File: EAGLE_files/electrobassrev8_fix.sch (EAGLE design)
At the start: 234 parts, among them IC1 CY8C58LPXXX, IC18 CY8C4124, IC2 4052D, IC3 LMV321M5, IC5 LMV321M5, IC6 LM324D, J1 105162-0001, J28 PJ-066A, Q1 DMP3099L, U1 ES_DAISY_SEED_DOUBLE, U2 LP2985, U7 ES_DAISY_SEED_DOUBLE, X1 3P-2MM-TH-MALE, X10 3P-2MM-TH-MALE, X11 3P-2MM-TH-MALE, X12 3P-2MM-TH-MALE, X13 3P-2MM-TH-MALE, X14 3P-2MM-TH-MALE, X15 3P-2MM-TH-MALE, X16 332-02, X17 332-02, X18 332-02, X19 332-02, X2 NRJ6HF2, X3 NRJ6HF2, X4 USB+SHIELD, X5 332-02, X6 332-02, X7 332-02, X8 332-02, X9 3P-2MM-TH-MALE

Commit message: changes to how presets are loaded
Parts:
- removed 0_6: (no value), adafruit:PINHD-1X1
- removed IC1: CY8C58LPXXX, cypress:CY8C58LPXXX
- removed JP17, JP18, JP19: PINHD-2X5, Connector:PINHD-2X5
- removed JP20, JP21: 20021121, custom:20021121
- removed R47, R51, R52, R53, R54: 0R_DNP, adafruit:R-US_R0603
- removed U$7: CY8CKIT-059_TARGET_3, CY8KIT-059:CY8CKIT-059_TARGET_3
- added 12VD1: (no value), adafruit:PINHD-1X1
- added C15, C19, C22, C23, C24, C25: 10uf, rcl:C-EUC1206K
- added C16, C31, C32, C33, C36, C45, C46: 1uf, rcl:C-EUC0603
- added C17: .001uf, rcl:C-EUC0603
- added C18: .01uf, adafruit:C-USC0603K
- added C20, C21: 22uf, rcl:C-EUC1206K
- added C26, C28, C30, C40, C41, C42, C43, C44: .1uf, rcl:C-USC0603K
- added C29: 2200pf, adafruit:C-USC0603K
- added J2, J3, J5, J6, J7, J8: SM06B-SRSS-TB(LF)(SN), sm06b:SM06B-SRSS-TB(LF)(SN)
- added JP5: 20021121, custom:20021121
- added L1: 2.2uH, Electrosmith-Passives:INDUCTORS
- added R27, R36: 20k, Resistor:R-US_R0603
- added R34, R35: 10k, Resistor:R-US_R0603
- added R37: 22R, rcl:R-US_R0603
- added R56, R57, R88, R89, R90: 2M, Electrosmith-Passives:R-US_R0603
- added R91, R92: 100R, Electrosmith-Passives:R-US_R0603
- added R93, R94, R95, R96, R97: 47k, rcl:R-US_R0603
- added U$9: POWER_ISOLATE, Electrosmith-IC:POWER_ISOLATE
- added U10: OPA1654, Electrosmith-IC:OPA1654_TSSOP-14
- added U3: MCP1755T-5002E/DCSOT-223_5_MCH-M, MCP1755T:MCP1755T-5002E/DCSOT-223_5_MCH-M
- added U4: CY8C5888LTI-LP097QFN-68-M, cy8c:CY8C5888LTI-LP097QFN-68-M
- added U5: ADUM3160BRWZRW_16_ADI-M, MCP1755T:ADUM3160BRWZRW_16_ADI-M
- R23: value 0R -> 2M; device adafruit:R-US_R0603 -> Electrosmith-Passives:R-US_R0603; PARTNO CRCW06030000Z0EAHP -> (none)
- R32: value 1.6k -> 5R_DNP; PARTNO ESR03EZPJ152 -> CRCW06030000Z0EAHP
- R41: value 1.6k -> 22R; device adafruit:R-US_R0603 -> rcl:R-US_R0603; PARTNO ESR03EZPJ152 -> RC0603JR-0747RL
- R45, R46: value 0R_DNP -> 22R; device adafruit:R-US_R0603 -> rcl:R-US_R0603; PARTNO *DNP -> RC0603JR-0747RL
- R50: value 0R -> 5R
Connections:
- net N$66 renamed ADC4OPAMPOUT
- removed net ADC1_2: R53.1, U7.GPIO15(ADC0)
- removed net ADC2_2: R51.1, U7.GPIO16(ADC1)
- removed net ADC3_2: R54.1, U7.GPIO17(ADC2)
- removed net ADC4_2: R52.1, U7.GPIO18(ADC3)
- removed net ADC5_1: U1.GPIO19(ADC4)
- removed net ADC5_2: U7.GPIO19(ADC4)
- removed net ADC6_1: U1.GPIO20(ADC5)
- removed net ADC6_2: U7.GPIO20(ADC5)
- removed net ADC7_1: U1.GPIO21(ADC6)
- removed net ADC7_2: U7.GPIO21(ADC6)
- removed net ADC8_1: U1.GPIO22(ADC7/DAC2)
- removed net ADC8_2: U7.GPIO22(ADC7/DAC2)
- removed net DAISY_D+: R45.1, U7.GPIO30(USB_HS_D+)
- removed net DAISY_D-: R47.1, U7.GPIO29(USB_HS_D_-)
- removed net EXTRA_GPIO: 0_6.1, U$7.P_0.6
- removed net PA0_VBUS: R23.1, U7.GPIO25(ADC10)
- removed net PICKUP2_OUT: JP19.2, JP21.P$10, JP21.P$9
- removed net PICKUP3_OUT: JP19.3, JP21.P$7, JP21.P$8
- removed net SCL_GN: R41.2, U1.GPIO11(I2C1_SCL), U7.GPIO11(I2C1_SCL)
- removed net SDA_GN: R32.2, U1.GPIO12(I2C1_SDA), U7.GPIO12(I2C1_SDA)
- new net +5V_ISOL: C20.1, C28.1, R23.2, R88.2, U$9.OUT+, U10P.V+
- new net 5V0: C15.1, C16.1, C17.1, C18.1, C21.1, L1.P$1, U3.VOUT
- new net ADC1OPAMPOUT: C4.2, IC6A.OUT, R1.1, R81.2
- new net ADC2OPAMPOUT: C9.2, IC6B.OUT, R24.1, R80.2
- new net ADC3OPAMPOUT: C10.2, IC6C.OUT, R26.1, R83.2
- new net ADCBYPASS: C31.1, U4.P0[3]_(GPIO
- new net AGND4: G1.1, JP15.4, JP15.6, X2.S
- new net CMOD_CH0: C29.1, U4.P15[4]_(GPIO)
- new net GNDINT: C20.2, C28.2, JP1.4, JP4.10, R32.1, R34.2, R35.2, R56.1, R57.1, R89.1, R90.1, U$9.OUT-, U10P.V-
- new net GNDINT_KNOBS: JP3.10, U$2.P$2, U$2.P$6
- new net GNDIO: C30.2, JP1.8, JP22.4, U5.GND1, U5.GND1_2
- new net LOUT_2_INTOCN: C24.2, JP4.4, R57.2
- new net N$20: R35.1, R36.2, U10B.-IN
- new net N$21: S1.1, S1.4
- new net N$23: R37.1, U5.UD-
- new net N$24: R41.1, U5.UD+
- new net N$63: R45.2, U5.DD-
- new net N$64: R46.2, U5.DD+
- new net N$76: R27.1, R91.2, U10A.OUT
- new net N$77: C23.2, R88.1, R89.2, U10B.+IN
- new net N$78: R36.1, R92.2, U10B.OUT
- new net N$79: C24.1, R91.1
- new net N$80: C25.1, R92.1
- new net N$81: C19.1, L1.P$2, U$9.IN+
- new net PROG_RESET: JP5.P$10, U4.XRES
- new net PROG_SWDCLK: JP5.P$4, U4.(TCK
- new net PROG_SWDIO: JP5.P$2, U4.(TMS
- new net PROG_SWO: JP5.P$6, U4.(TDO
- new net ROUT_2_INTOCN: C25.2, JP4.2, R90.2
- new net SPI_READY: U1.GPIO6(SDMMC1_CK), U4.P0[6]_(GPIO, U7.GPIO0(USB_HS_ID)
- new net USBDM: R45.1, U4.(USBIO
- new net USBDP: R46.1, U4.(USBIO_2
- new net VCCA_1: C32.1, C42.1, U4.VCCA
- new net VCCD_1: C36.1, C40.1, U4.VCCD, U4.VCCD_2
- net +10V: now also J2.3, J2.4, J3.3, J3.4; no longer JP18.7, JP18.9
- net +3V3: now also C26.1, C43.1, C44.1, C45.1, C46.1, R93.2, R94.2, R95.2, R96.2, R97.2, U4.VDDD, U4.VDDD_2, U4.VDDIO0, U4.VDDIO1, U4.VDDIO2, U4.VDDIO3, U5.PIN, U5.SPD, U5.VBUS2, U5.VDD2; no longer R32.1, R41.1, U$7.VDD, U$7.VDDIO
- net 12VD1: now also 12VD1.1, U3.!SHDN, U3.VIN
- net 3V3A1: now also C33.1, C41.1, U4.VDDA; no longer R46.1
- net 3V3FORPEDAL: now also JP1.9; no longer JP1.7
- net ADC1_1: no longer C4.2, IC6A.OUT, R1.1, R53.2, R81.2
- net ADC2_1: no longer C9.2, IC6B.OUT, R24.1, R51.2, R80.2
- net ADC3_1: no longer C10.2, IC6C.OUT, R26.1, R54.2, R83.2
- net ADC4_1: no longer R52.2
- net AGND: now also C15.2, C16.2, C17.2, C18.2, C19.2, C21.2, C31.2, C32.2, C33.2, C41.2, C42.2, J2.2, J2.5, J3.2, J3.5, JP1.7, R32.2, U$9.IN-, U3.GND, U4.VSSA; no longer JP1.4, JP1.8, JP18.10, JP18.8, JP4.10, S1.1, S1.4
- net AGND3: now also JP15.7; no longer G1.1, JP15.4, JP15.6, X2.S
- net BLUE_LED: now also U4.P2[1]_(GPIO); no longer U$7.P_2.1
- net CAP_0_0: now also U4.P2[0]_(GPIO); no longer U$7.P_2.0
- net CAP_0_1: now also U4.P2[2]_(GPIO); no longer U$7.P_2.2
- net CAP_0_2: now also U4.P2[4]_(GPIO; no longer U$7.P_2.4
- net CAP_0_3: now also U4.(TRACEDATA[2]; no longer U$7.P_2.6
- net CAP_1_0: now also U4.(IDAC1; no longer U$7.P_3.0
- net CAP_1_1: now also U4.(OPAMP3+; no longer U$7.P_3.3
- net CAP_1_2: now also U4.(OPAMP1+; no longer U$7.P_3.5
- net CAP_1_3: now also U4.P3[7]_(GPIO; no longer U$7.P_3.7
- net CMOD_CH1: now also U4.(TDI; no longer U$7.P_1.4
- net CV_PEDAL: now also U4.(OPAMP1-; no longer U$7.P_3.4
- net CV_PEDAL_SENSE: now also U4.(OPAMP3-; no longer U$7.P_3.2
- net DGND: now also C26.2, C29.2, C36.2, C40.2, C43.2, C44.2, C45.2, C46.2, JP5.P$3, JP5.P$5, JP5.P$7, JP5.P$9, U4.EPAD, U4.VBAT, U4.VBOOST, U4.VSSB, U4.VSSD, U4.VSSD_2, U4.VSSD_3, U4.VSSD_4, U5.GND2, U5.GND2_2; no longer JP1.9, JP22.4, U$7.GND1, U$7.GND2, U$7.GND3
- net DGND3: no longer JP15.9
- net DM: now also R37.2; no longer R47.2
- net DOWN: now also U4.P15[3]_(GPIO; no longer U$7.P_15.3
- net DP: now also R41.2; no longer R45.2
- net EDIT: now also U4.P15[2]_(GPIO; no longer U$7.P_15.2
- net EXT_MUX_EN: now also U4.P15[5]_(GPOI); no longer U$7.P_15.5
- net EXT_MUX_S0: now also U4.(MHZ_XTAL:_XO; no longer U$7.P_15.0
- net EXT_MUX_S1: now also U4.(MHZ_XTAL:_XI; no longer U$7.P_15.1
- net FRETTED_LATCHING: now also U4.P12[3]_(SIO); no longer U$7.P_12.3
- net FRETTED_MOMENTARY: now also U4.P12[2]_(SIO); no longer U$7.P_12.2
- net IDAC_OUT: now also U4.P0[7]_(GPIO; no longer U$7.P_0.7
- net JOY_X: now also U4.P2[5]_(GPIO; no longer U$7.P_2.5
- net JOY_Y: now also U4.P2[3]_(GPIO; no longer U$7.P_2.3
- net KNOB_1: now also U4.P0[1]_(GPIO; no longer U$7.P_0.1
- net KNOB_2: now also U4.P3[6]_(GPIO; no longer U$7.P_3.6
- net LED_1: now also U4.P0[2]_(GPIO; no longer U$7.P_0.2
- net LOUT_2: now also C22.1; no longer JP4.4
- net MISO_1: now also U4.(GPIO)_P1[7]; no longer U$7.P_1.7
- net MISO_2: now also U4.(TRACEDATA[3]; no longer U$7.P_2.7
- net MOSI_1_P: now also U4.(SIO)_P12[6]; no longer U$7.P_12.6
- net MOSI_2_P: now also U4.(I2C0:_SCL; no longer U$7.P_12.4
- net N$45: no longer R46.2
- net N$56: now also JP15.9; no longer JP15.7
- net N$7: now also C22.2, R23.1, R56.2, U10A.+IN; no longer U1.GPIO26(SAI2_SD_A), U7.GPIO26(SAI2_SD_A)
- net N$8: now also R27.2, R34.1, U10A.-IN; no longer U1.GPIO27(SAI2_FS_B), U7.GPIO27(SAI2_FS_B)
- net OUTGND: no longer JP3.10, U$2.P$2, U$2.P$6
- net PICKUP1: now also J3.6; no longer JP18.1
- net PICKUP1_OUT: now also J6.6; no longer JP19.1
- net PICKUP1_OUT2: now also J7.6; no longer JP17.1
- net PICKUP2: now also J2.6; no longer JP18.2
- net PICKUP2_OUT2: now also J8.6; no longer JP17.2
- net PICKUP2_OUT_HIGH: now also J5.6; no longer JP20.P$10, JP20.P$9
- net PICKUP3: now also J2.1; no longer JP18.3
- net PICKUP3_OUT2: now also J8.1; no longer JP17.3
- net PICKUP3_OUT_HIGH: now also J5.1; no longer JP20.P$7, JP20.P$8
- net PICKUP4: now also J3.1; no longer JP18.4
- net PICKUP4_OUT: now also J6.1; no longer JP19.4
- net PICKUP4_OUT2: now also J7.1; no longer JP17.4
- net PICKUP_GND1: now also J6.2, J6.5; no longer JP19.10, JP19.8, JP21.P$1, JP21.P$2, JP21.P$3, JP21.P$4
- net PICKUP_GND1_HIGH: now also J5.2, J5.5; no longer JP20.P$1, JP20.P$2, JP20.P$3, JP20.P$4
- net PICKUP_GND2: now also J7.2, J7.5, J8.2, J8.5; no longer JP17.10, JP17.8
- net PICKUP_PWR1: now also J6.3, J6.4; no longer JP19.7, JP19.9, JP21.P$5, JP21.P$6
- net PICKUP_PWR1_HIGH: now also J5.3, J5.4; no longer JP20.P$5, JP20.P$6
- net PICKUP_PWR2: now also J7.3, J7.4, J8.3, J8.4; no longer JP17.7, JP17.9
- net ROUT_2: now also C23.1; no longer JP4.2
- net SCL: now also U4.P12[0]_(SIO; no longer U$7.P_12.0
- net SCLK_1_P: now also U4.(GPIO)_P1[6]; no longer U$7.P_1.6
- net SCLK_2_P: now also U4.(I2C0:_SDA; no longer U$7.P_12.5
- net SDA: now also U4.P12[1]_(SIO; no longer U$7.P_12.1
- net SD_CMD: now also R95.1
- net SD_DAT0: now also R94.1
- net SD_DAT1: now also R93.1
- net SD_DAT2: now also R97.1
- net SD_DAT3: now also R96.1
- net SS_1_P: now also U4.(NTRST; no longer U$7.P_1.5
- net SS_2_P: now also U4.(CONFIGURABLE_XRES; no longer U$7.P_1.2
- net UP: now also U4.(IDAC3; no longer U$7.P_3.1
- net VBUS: now also C30.1, U5.PDEN, U5.SPU, U5.VBUS1, U5.VDD1
- net VBUS_DIVIDED: now also U4.(SIO)_P12[7]; no longer R23.2, U$7.P_12.7
- net V_H: now also U4.P0[4]_(GPIO; no longer U$7.P_0.4
- net V_T: now also U4.P0[0]_(GPIO, U4.P0[5]_(GPIO; no longer U$7.P_0.0, U$7.P_0.5
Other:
- note added: "Audio"
- note added: "Buffers the output signal Biased at 2V5"
- moved on the sheet: AGND5, DGND, DGND1, R10, R41, R45, R46, R8

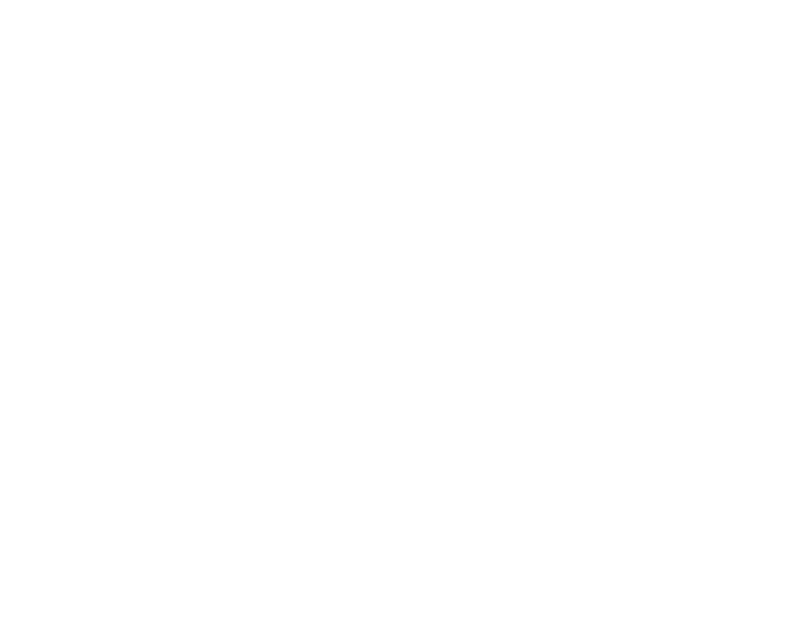
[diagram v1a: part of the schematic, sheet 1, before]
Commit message: writing multiple presets to an sd card and loading them based on commands from psoc
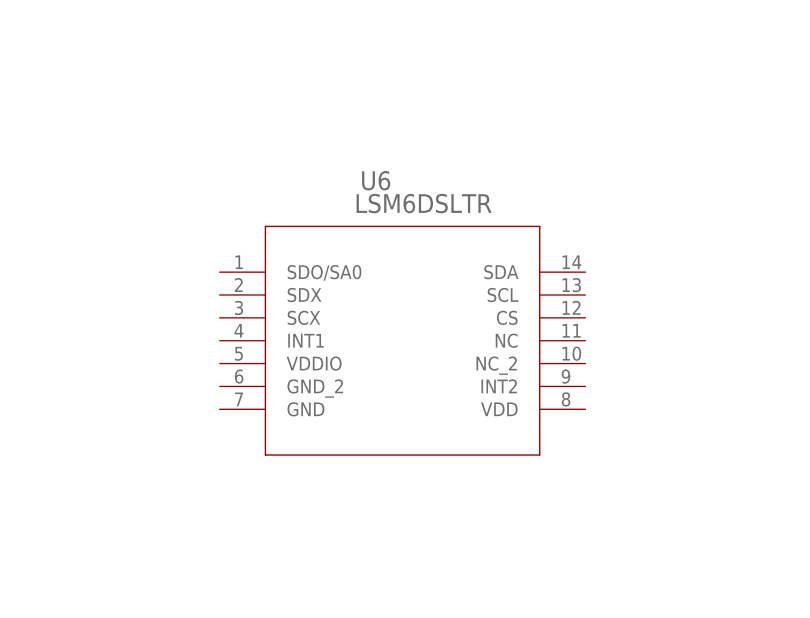
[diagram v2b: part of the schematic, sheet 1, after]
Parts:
- added U6: LSM6DSLTR, 6dsl:LSM6DSLTR
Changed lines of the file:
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@@
 </part>
 <part name="V17" library="custom" deviceset="3V3A1" device=""/>
+<part name="U6" library="6dsl" deviceset="LSM6DSLTR" device=""/>
 </parts>
 <sheets>
@@
 <attribute name="VALUE" x="462.28" y="29.845" size="1.778" layer="96" ratio="12"/>
 </instance>
+<instance part="U6" gate="A" x="530.86" y="45.72" smashed="yes">
+<attribute name="NAME" x="548.9956" y="54.8386" size="2.0828" layer="95" ratio="6" rot="SR0"/>
+<attribute name="VALUE" x="548.3606" y="52.2986" size="2.0828" layer="96" ratio="6" rot="SR0"/>
+</instance>
 </instances>
